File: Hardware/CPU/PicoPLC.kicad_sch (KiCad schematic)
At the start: 91 parts, among them J1 Input cluster 0, J2 Input cluster 1, J3 Common terminals, J4 C0 terminal, J5 C1 terminal, J6 C2 terminal, J7 C3 terminal, K1 SANYOU_SRD_Form_C, K2 SANYOU_SRD_Form_C, K3 SANYOU_SRD_Form_C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

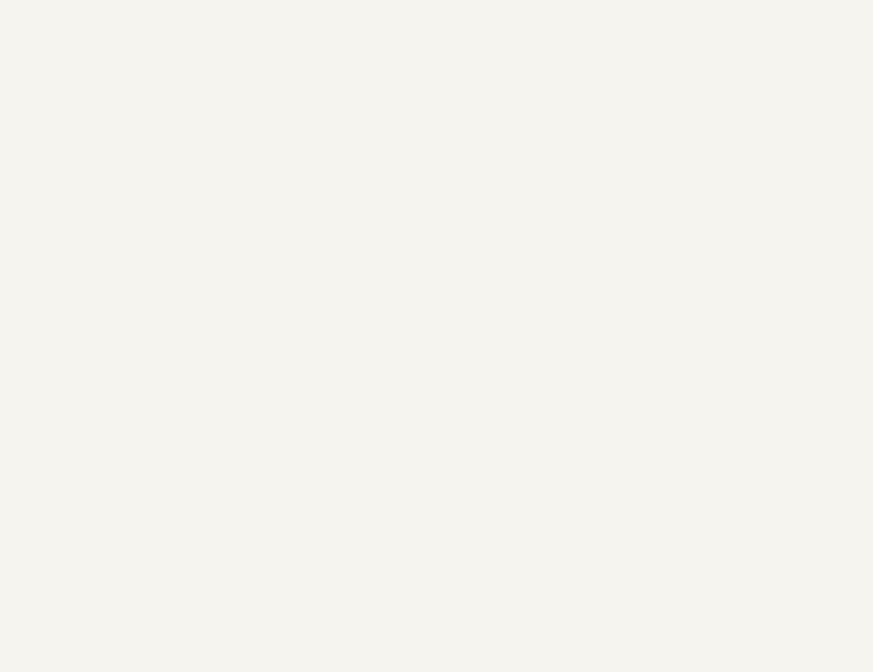
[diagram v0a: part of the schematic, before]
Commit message: working on screen capabilities
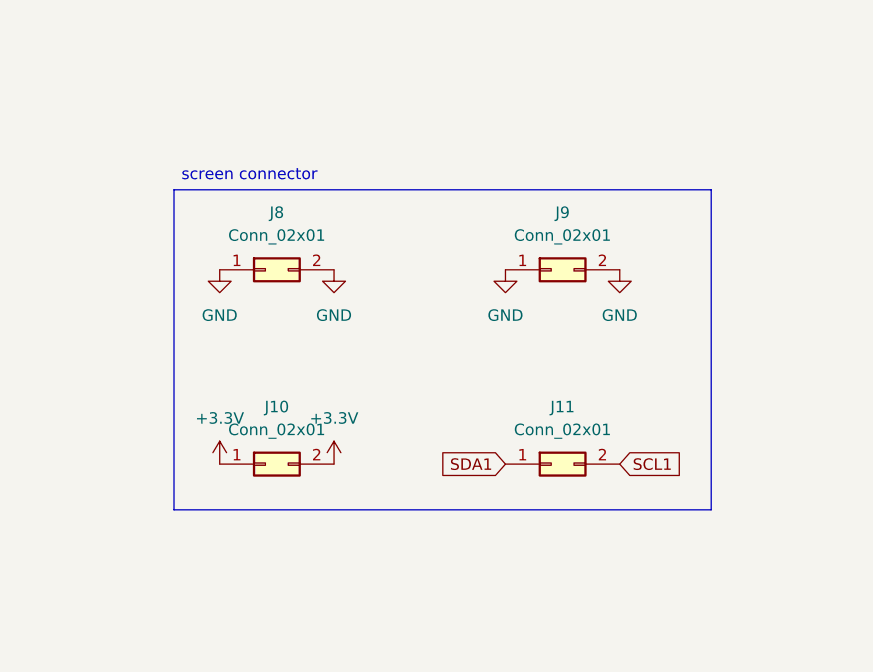
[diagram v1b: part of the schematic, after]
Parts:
- added J10, J11, J9: Conn_02x01, symbol Connector_Generic:Conn_02x01
- added J8: Conn_02x01, Connector_PinHeader_2.54mm:PinHeader_2x01_P2.54mm_Vertical, symbol Connector_Generic:Conn_02x01
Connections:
- net +3.3V: now also J10.1 (Pin_1), J10.2 (Pin_2)
- net GND: now also J8.1 (Pin_1), J8.2 (Pin_2), J9.1 (Pin_1), J9.2 (Pin_2)
- net SCL1: now also J11.2 (Pin_2)
- net SDA1: now also J11.1 (Pin_1)
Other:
- note added: "screen connector"
